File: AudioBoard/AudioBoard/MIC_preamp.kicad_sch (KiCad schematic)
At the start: 30 parts, among them U2 NE5532, U3 NE5532

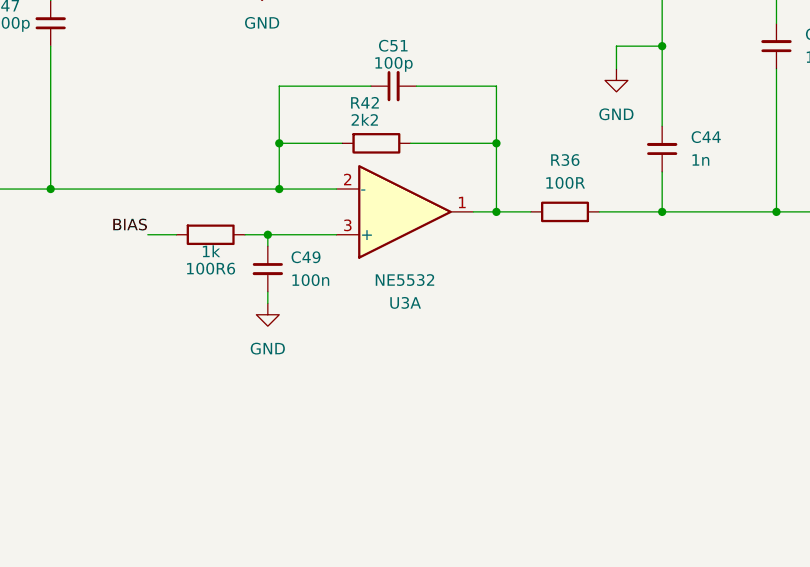
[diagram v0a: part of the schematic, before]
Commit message: added first time routing to see crosssections
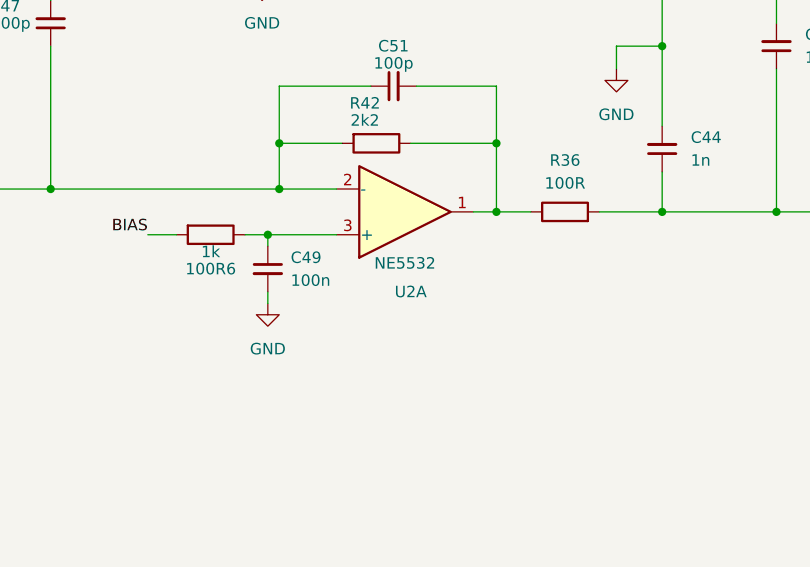
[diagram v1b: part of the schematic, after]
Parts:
- renumbered U3 to U2
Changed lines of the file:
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@@
 		(in_pos_files yes)
 		(dnp no)
-		(fields_autoplaced yes)
-		(property "Reference" "U3"
-			(at 159.385 102.87 0)
+		(property "Reference" "U2"
+			(at 160.02 101.6 0)
 			(show_name no)
 			(do_not_autoplace no)
@@
 		)
 		(property "Value" "NE5532"
-			(at 159.385 100.33 0)
+			(at 159.385 98.425 0)
 			(show_name no)
 			(do_not_autoplace no)
@@
 			(project "AudioBoard"
 				(path "/dd5d876d-fff7-4cb4-baee-a023036d12ae/07626587-873c-4131-ae5a-c23e8e886a82"
-					(reference "U3")
+					(reference "U2")
 					(unit 1)
 				)

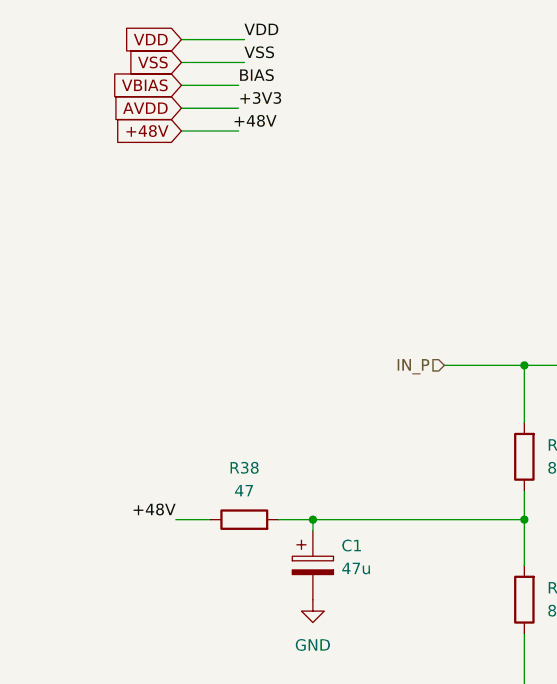
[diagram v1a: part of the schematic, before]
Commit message: added power electronics
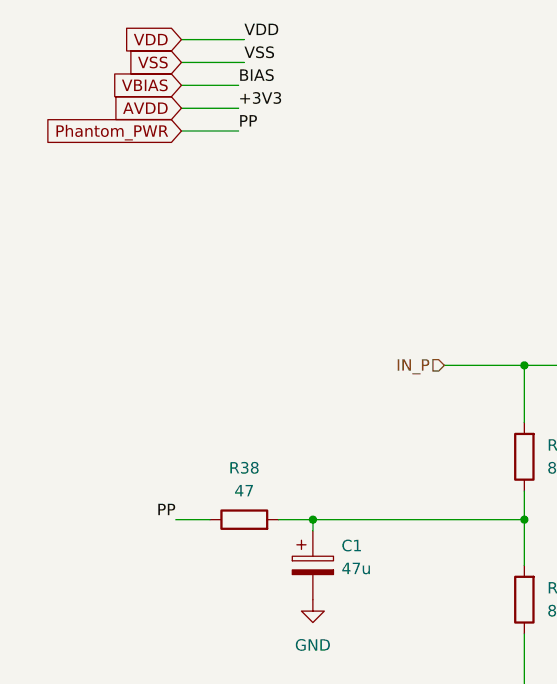
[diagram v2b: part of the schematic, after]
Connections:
- net +48V renamed Phantom_PWR
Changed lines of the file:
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@@
 		)
 	)
-	(label "+48V"
-		(at 45.085 27.94 0)
+	(label "PP"
+		(at 45.72 27.94 0)
 		(effects
 			(font
@@
 		)
 	)
-	(label "+48V"
+	(label "PP"
 		(at 38.735 71.12 180)
 		(effects
@@
 		)
 	)
-	(global_label "+48V"
+	(global_label "Phantom_PWR"
 		(shape input)
 		(at 39.37 27.94 180)
@@
 		)
 		(property "Intersheetrefs" "${INTERSHEET_REFS}"
-			(at 31.3048 27.94 0)
+			(at 23.1408 27.94 0)
 			(hide yes)
 			(show_name no)

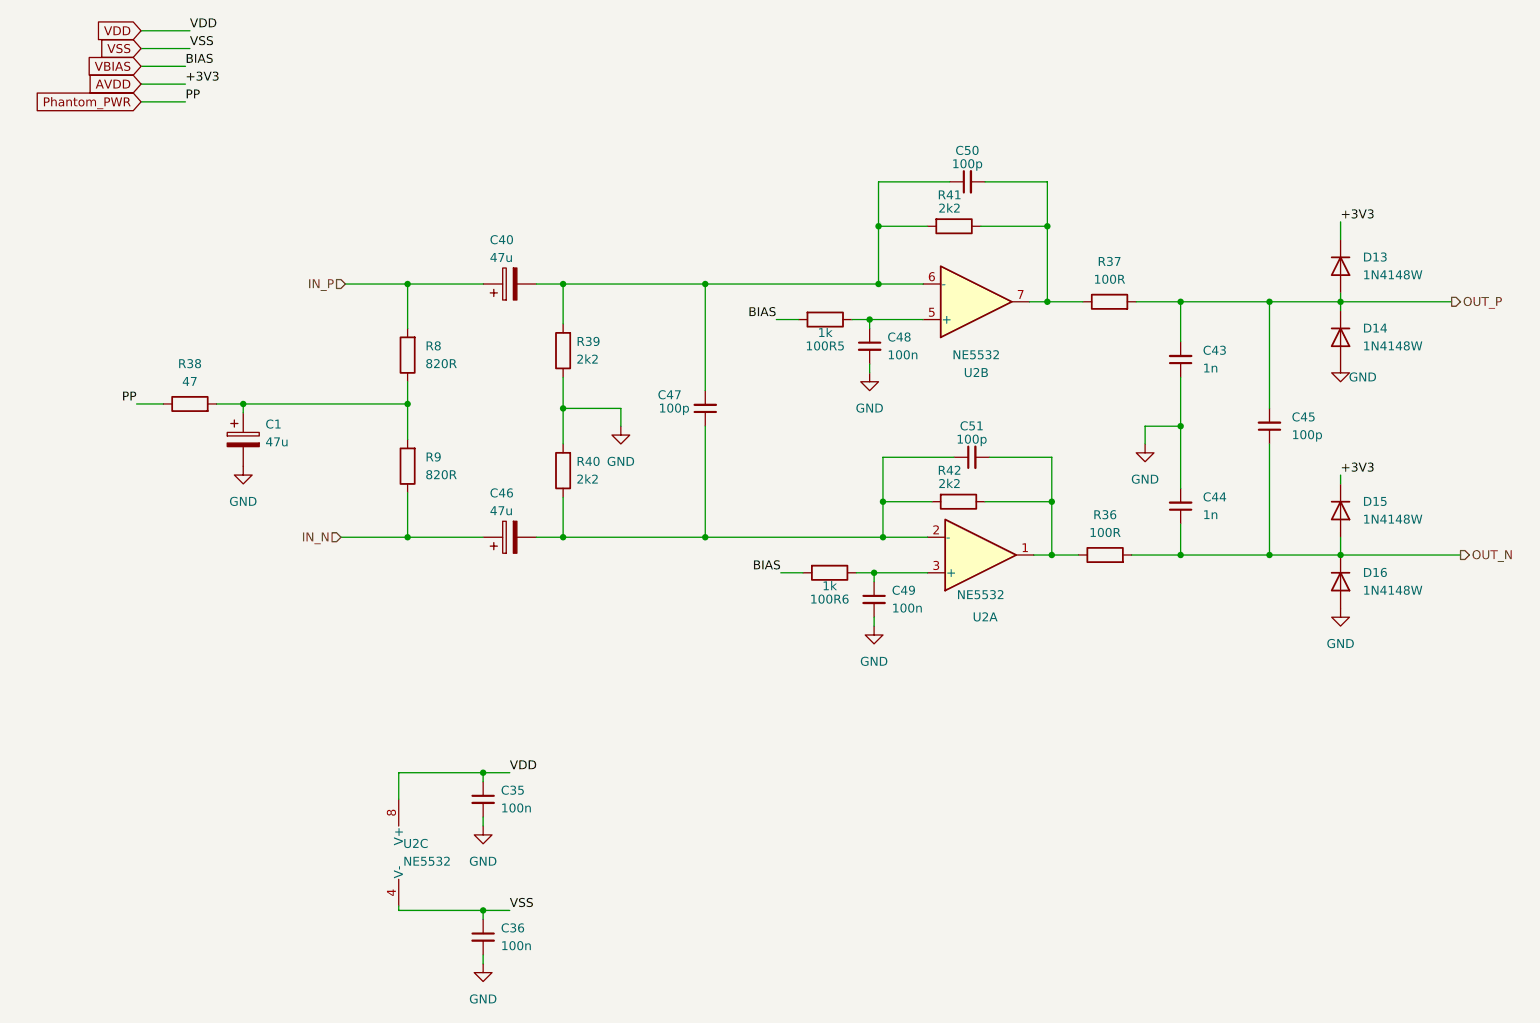
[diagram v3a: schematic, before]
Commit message: modified clamping diodes on inputs, added exp pedal input filter, added ideas to instrument input filter redesign
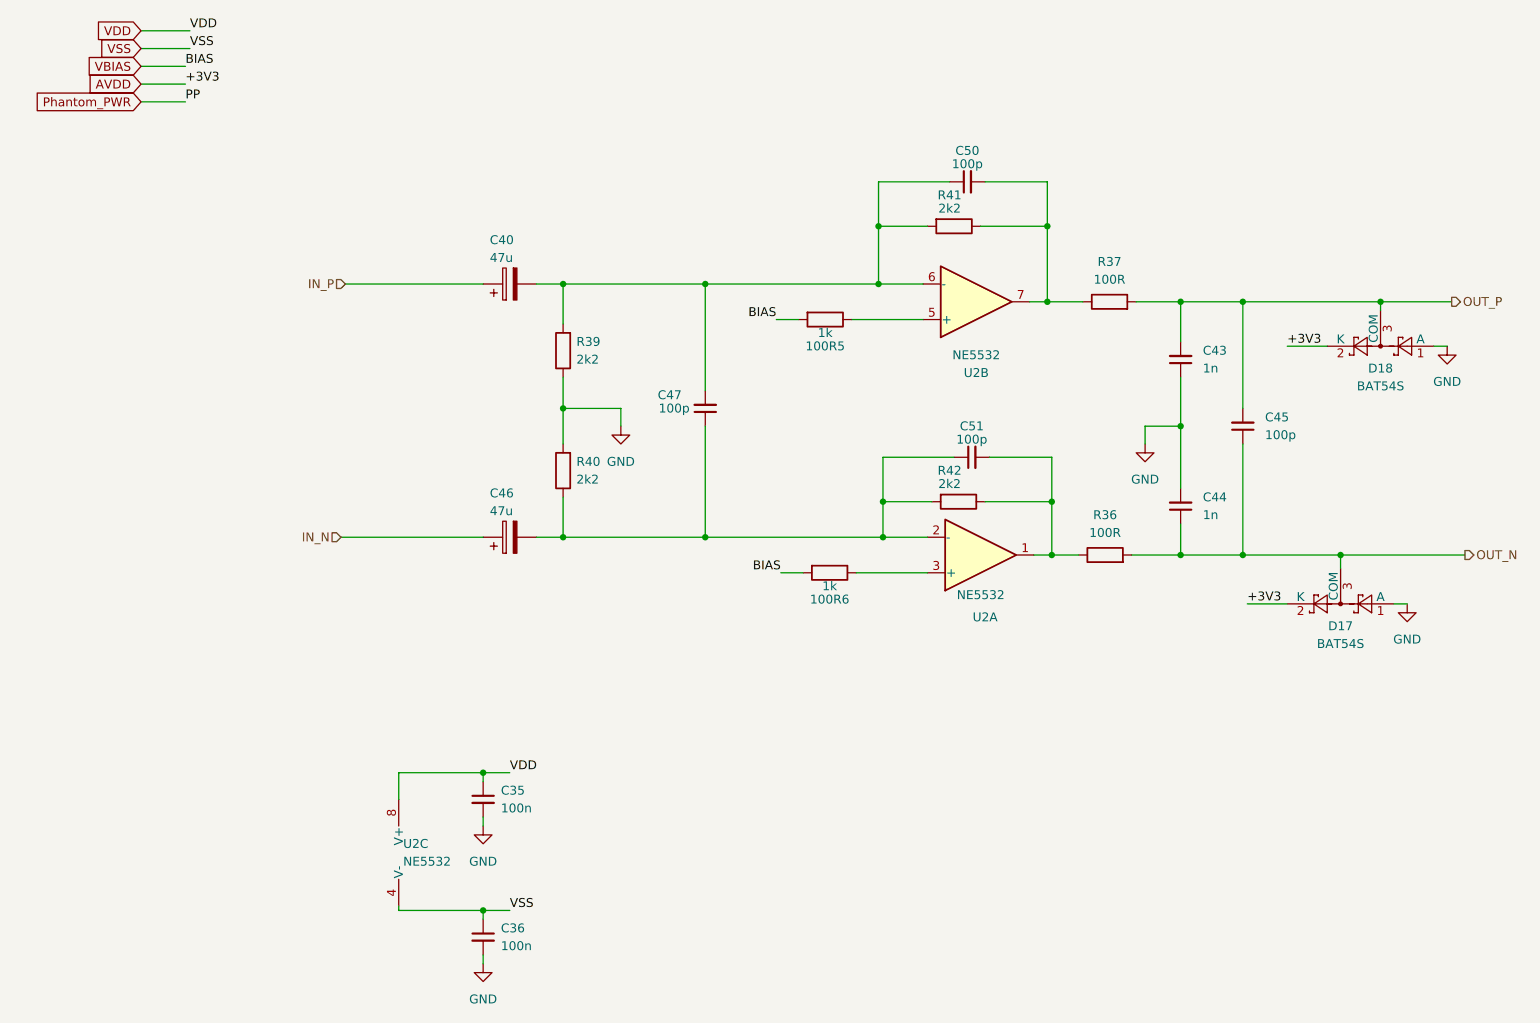
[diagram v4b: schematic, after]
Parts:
- removed C1: 47u, Capacitor_THT:CP_Radial_D6.3mm_P2.50mm, symbol Device:C_Polarized
- removed C48, C49: 100n, Capacitor_SMD:C_0402_1005Metric, symbol Device:C_Small
- removed D13, D14, D15, D16: 1N4148W, Diode_SMD:D_SOD-123, symbol Diode:1N4148W
- removed R38: 47, Resistor_SMD:R_0603_1608Metric, symbol Device:R
- removed R8, R9: 820R, Resistor_SMD:R_0603_1608Metric, symbol Device:R
- added D17, D18: BAT54S, Package_TO_SOT_SMD:SOT-23, symbol Diode:BAT54S
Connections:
- net AVDD: now also D17.2 (K), D18.2 (K)
- net GND: now also D17.1 (A), D18.1 (A)
- net OUT_N: now also D17.3 (COM)
- net OUT_P: now also D18.3 (COM)
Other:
- moved on the sheet: C45
